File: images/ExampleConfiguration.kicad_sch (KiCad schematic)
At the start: 11 parts, among them U1 ProMicro, U2 RC_Receiver, U3 BMP280, U4 NEO_GPS, U5 ACS756xCB-050B-PFF

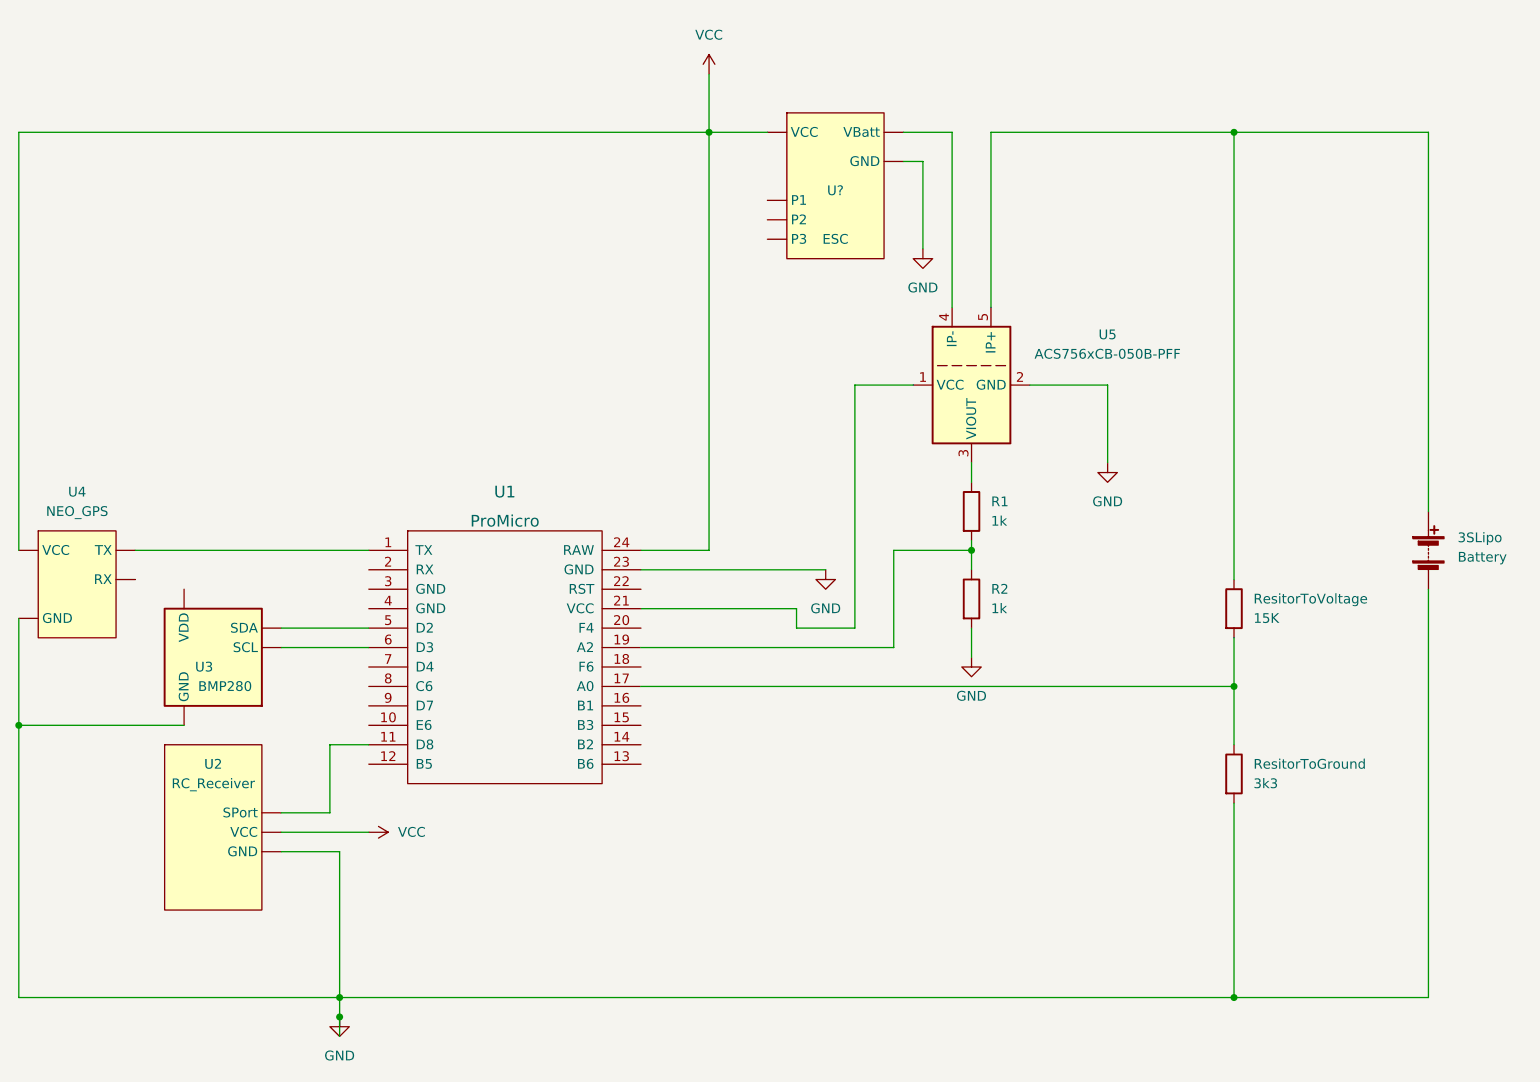
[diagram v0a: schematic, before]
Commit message: Added Labels with voltage values
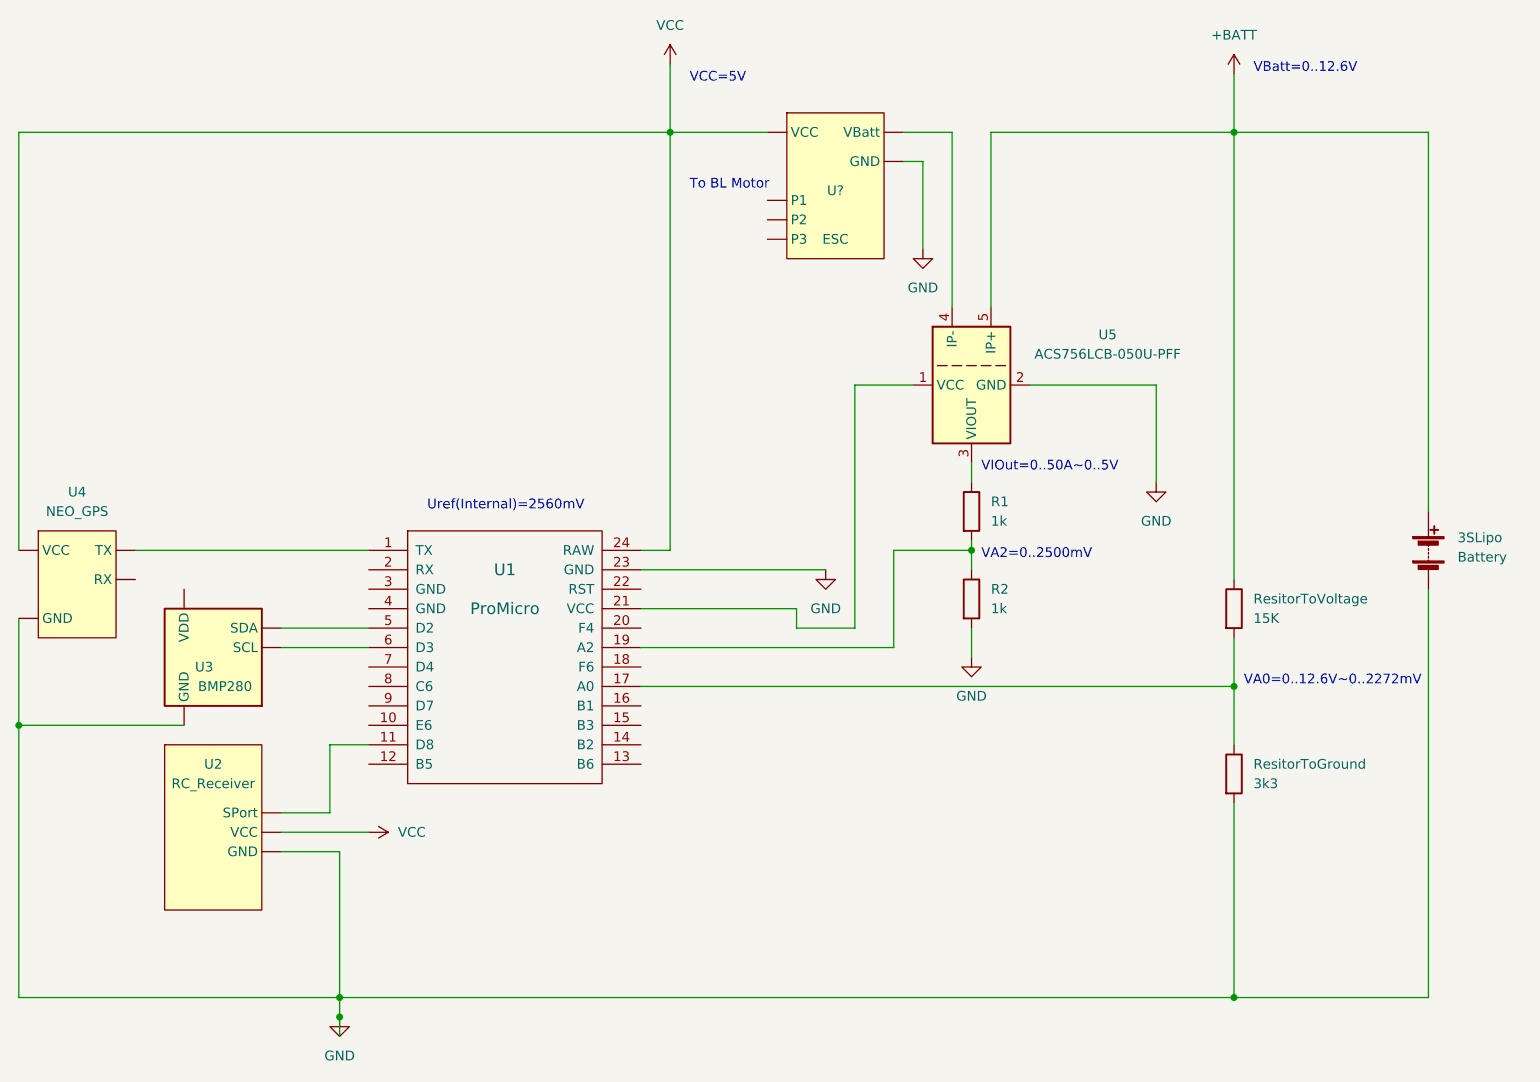
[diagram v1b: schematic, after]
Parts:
- U5: value ACS756xCB-050B-PFF -> ACS756LCB-050U-PFF
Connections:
- net +BATT: now reaches 3SLipo.1 (+), ResitorToVoltage.1, U5.5 (IP-)
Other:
- note added: "To BL Motor"
- note added: "Uref(Internal)=2560mV"
- note added: "VA0=0..12.6V~0..2272mV"
- note added: "VA2=0..2500mV"
- note added: "VBatt=0..12.6V"
- note added: "VCC=5V"
- note added: "VIOut=0..50A~0..5V"
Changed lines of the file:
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@@
   (junction (at 179.07 83.82) (diameter 0) (color 0 0 0 0)
   )
-  (junction (at 144.78 29.21) (diameter 0) (color 0 0 0 0)
-  )
   (junction (at 96.52 142.24) (diameter 0) (color 0 0 0 0)
   )
@@
   (junction (at 54.61 106.68) (diameter 0) (color 0 0 0 0)
   )
+  (junction (at 139.7 29.21) (diameter 0) (color 0 0 0 0)
+  )
   (junction (at 213.36 29.21) (diameter 0) (color 0 0 0 0)
   )
@@
     (stroke (width 0) (type default) (color 0 0 0 1))
   )
-  (wire (pts (xy 196.85 62.23) (xy 196.85 72.39))
+  (wire (pts (xy 203.2 62.23) (xy 203.2 74.93))
     (stroke (width 0) (type default) (color 0 0 0 1))
   )
@@
     (stroke (width 0) (type default) (color 0 0 0 0))
   )
+  (wire (pts (xy 54.61 29.21) (xy 139.7 29.21))
+    (stroke (width 0) (type default) (color 255 0 0 1))
+  )
   (wire (pts (xy 213.36 29.21) (xy 213.36 87.63))
     (stroke (width 0) (type default) (color 255 0 0 1))
@@
     (stroke (width 0) (type default) (color 0 0 0 0))
   )
-  (wire (pts (xy 144.78 29.21) (xy 144.78 83.82))
-    (stroke (width 0) (type default) (color 255 0 0 1))
-  )
-  (wire (pts (xy 144.78 29.21) (xy 144.78 21.59))
+  (wire (pts (xy 139.7 29.21) (xy 139.7 83.82))
+    (stroke (width 0) (type default) (color 255 0 0 1))
+  )
+  (wire (pts (xy 139.7 29.21) (xy 139.7 20.32))
     (stroke (width 0) (type default) (color 255 0 0 1))
   )
@@
     (stroke (width 0) (type default) (color 0 0 0 0))
   )
-  (wire (pts (xy 144.78 83.82) (xy 135.89 83.82))
-    (stroke (width 0) (type default) (color 255 0 0 1))
-  )
   (wire (pts (xy 213.36 109.22) (xy 213.36 101.6))
     (stroke (width 0) (type default) (color 0 0 0 0))
@@
     (stroke (width 0) (type default) (color 0 0 0 0))
   )
-  (wire (pts (xy 186.69 62.23) (xy 196.85 62.23))
-    (stroke (width 0) (type default) (color 0 0 0 1))
+  (wire (pts (xy 186.69 62.23) (xy 203.2 62.23))
+    (stroke (width 0) (type default) (color 0 0 0 1))
+  )
+  (wire (pts (xy 213.36 21.59) (xy 213.36 29.21))
+    (stroke (width 0) (type default) (color 255 0 0 1))
   )
   (wire (pts (xy 179.07 82.55) (xy 179.07 83.82))
@@
     (stroke (width 0) (type default) (color 0 0 0 1))
   )
-  (wire (pts (xy 144.78 29.21) (xy 54.61 29.21))
-    (stroke (width 0) (type default) (color 255 0 0 1))
-  )
   (wire (pts (xy 213.36 29.21) (xy 238.76 29.21))
     (stroke (width 0) (type default) (color 255 0 0 1))
   )
-  (wire (pts (xy 144.78 29.21) (xy 152.4 29.21))
+  (wire (pts (xy 139.7 83.82) (xy 135.89 83.82))
+    (stroke (width 0) (type default) (color 255 0 0 1))
+  )
+  (wire (pts (xy 139.7 29.21) (xy 152.4 29.21))
     (stroke (width 0) (type default) (color 255 0 0 1))
   )
@@
   (wire (pts (xy 96.52 144.78) (xy 96.52 147.32))
     (stroke (width 0) (type default) (color 0 0 0 0))
+  )
+  (text "VCC=5V" (at 142.24 22.86 0)
+    (effects (font (size 1.27 1.27)) (justify left bottom))
+  )
+  (text "VA0=0..12.6V~0..2272mV" (at 214.63 101.6 0)
+    (effects (font (size 1.27 1.27)) (justify left bottom))
+  )
+  (text "VA2=0..2500mV" (at 180.34 85.09 0)
+    (effects (font (size 1.27 1.27)) (justify left bottom))
+  )
+  (text "VBatt=0..12.6V" (at 215.9 21.59 0)
+    (effects (font (size 1.27 1.27)) (justify left bottom))
+  )
+  (text "To BL Motor" (at 142.24 36.83 0)
+    (effects (font (size 1.27 1.27)) (justify left bottom))
+  )
+  (text "Uref(Internal)=2560mV" (at 107.95 78.74 0)
+    (effects (font (size 1.27 1.27)) (justify left bottom))
+  )
+  (text "VIOut=0..50A~0..5V" (at 180.34 73.66 0)
+    (effects (font (size 1.27 1.27)) (justify left bottom))
   )
   (symbol (lib_id "Sensor_Pressure:BMP280") (at 80.01 99.06 0) (mirror y) (unit 1)
@@
     (pin "1")
   )
+  (symbol (lib_id "power:+BATT") (at 213.36 21.59 0) (unit 1)
+    (in_bom yes) (on_board yes) (fields_autoplaced)
+    (property "Reference" "#PWR?" (id 0) (at 213.36 25.4 0)
+      (effects (font (size 1.27 1.27)) hide)
+    )
+    (property "Value" "+BATT" (id 1) (at 213.36 16.51 0))
+    (property "Footprint" "" (id 2) (at 213.36 21.59 0)
+      (effects (font (size 1.27 1.27)) hide)
+    )
+    (property "Datasheet" "" (id 3) (at 213.36 21.59 0)
+      (effects (font (size 1.27 1.27)) hide)
+    )
+    (pin "1")
+  )
   (symbol (lib_id "Sensor_Current:ACS756xCB-050B-PFF") (at 179.07 62.23 90) (mirror x) (unit 1)
     (in_bom yes) (on_board yes) (fields_autoplaced)
     (property "Reference" "U5" (id 0) (at 196.85 55.6512 90))
-    (property "Value" "ACS756xCB-050B-PFF" (id 1) (at 196.85 58.1912 90))
+    (property "Value" "ACS756LCB-050U-PFF" (id 1) (at 196.85 58.1912 90))
     (property "Footprint" "Sensor_Current:Allegro_CB_PFF" (id 2) (at 179.07 62.23 0)
       (effects (font (size 1.27 1.27)) hide)
@@
     (pin "2")
   )
-  (symbol (lib_id "power:VCC") (at 144.78 21.59 0) (unit 1)
-    (in_bom yes) (on_board yes) (fields_autoplaced)
-    (property "Reference" "#PWR?" (id 0) (at 144.78 25.4 0)
-      (effects (font (size 1.27 1.27)) hide)
-    )
-    (property "Value" "VCC" (id 1) (at 144.78 16.51 0))
-    (property "Footprint" "" (id 2) (at 144.78 21.59 0)
-      (effects (font (size 1.27 1.27)) hide)
-    )
-    (property "Datasheet" "" (id 3) (at 144.78 21.59 0)
+  (symbol (lib_id "power:VCC") (at 139.7 20.32 0) (unit 1)
+    (in_bom yes) (on_board yes) (fields_autoplaced)
+    (property "Reference" "#PWR?" (id 0) (at 139.7 24.13 0)
+      (effects (font (size 1.27 1.27)) hide)
+    )
+    (property "Value" "VCC" (id 1) (at 139.7 15.24 0))
+    (property "Footprint" "" (id 2) (at 139.7 20.32 0)
+      (effects (font (size 1.27 1.27)) hide)
+    )
+    (property "Datasheet" "" (id 3) (at 139.7 20.32 0)
       (effects (font (size 1.27 1.27)) hide)
     )
@@
   )
   (symbol (lib_id "PrMicro:ProMicro") (at 118.11 102.87 0) (unit 1)
-    (in_bom yes) (on_board yes) (fields_autoplaced)
-    (property "Reference" "U1" (id 0) (at 118.11 76.2 0)
+    (in_bom yes) (on_board yes)
+    (property "Reference" "U1" (id 0) (at 118.11 86.36 0)
       (effects (font (size 1.524 1.524)))
     )
-    (property "Value" "ProMicro" (id 1) (at 118.11 80.01 0)
+    (property "Value" "ProMicro" (id 1) (at 118.11 91.44 0)
       (effects (font (size 1.524 1.524)))
     )
@@
     (pin "2")
   )
-  (symbol (lib_id "power:GND") (at 196.85 72.39 0) (unit 1)
-    (in_bom yes) (on_board yes) (fields_autoplaced)
-    (property "Reference" "#PWR?" (id 0) (at 196.85 78.74 0)
-      (effects (font (size 1.27 1.27)) hide)
-    )
-    (property "Value" "GND" (id 1) (at 196.85 77.47 0))
-    (property "Footprint" "" (id 2) (at 196.85 72.39 0)
-      (effects (font (size 1.27 1.27)) hide)
-    )
-    (property "Datasheet" "" (id 3) (at 196.85 72.39 0)
+  (symbol (lib_id "power:GND") (at 203.2 74.93 0) (unit 1)
+    (in_bom yes) (on_board yes) (fields_autoplaced)
+    (property "Reference" "#PWR?" (id 0) (at 203.2 81.28 0)
+      (effects (font (size 1.27 1.27)) hide)
+    )
+    (property "Value" "GND" (id 1) (at 203.2 80.01 0))
+    (property "Footprint" "" (id 2) (at 203.2 74.93 0)
+      (effects (font (size 1.27 1.27)) hide)
+    )
+    (property "Datasheet" "" (id 3) (at 203.2 74.93 0)
       (effects (font (size 1.27 1.27)) hide)
     )
@@
       (reference "#PWR?") (unit 1) (value "GND") (footprint "")
     )
+    (path "/1cea30eb-2532-4456-9a78-88cc39abe490"
+      (reference "#PWR?") (unit 1) (value "+BATT") (footprint "")
+    )
     (path "/295bdf11-c7f9-4654-a560-abaee7dc3d3f"
       (reference "#PWR?") (unit 1) (value "VCC") (footprint "")
@@
     )
     (path "/1da79c45-7d21-4f08-917b-f7cac88244f9"
-      (reference "U5") (unit 1) (value "ACS756xCB-050B-PFF") (footprint "Sensor_Current:Allegro_CB_PFF")
+      (reference "U5") (unit 1) (value "ACS756LCB-050U-PFF") (footprint "Sensor_Current:Allegro_CB_PFF")
     )
     (path "/e046c682-c5db-4c7d-a510-0488f5e3e3cb"
